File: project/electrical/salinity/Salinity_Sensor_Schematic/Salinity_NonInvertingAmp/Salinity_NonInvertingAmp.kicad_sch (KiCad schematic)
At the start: 13 parts, among them U1 MCP6L01, U2 MCP6L01, U3 MCP6L01

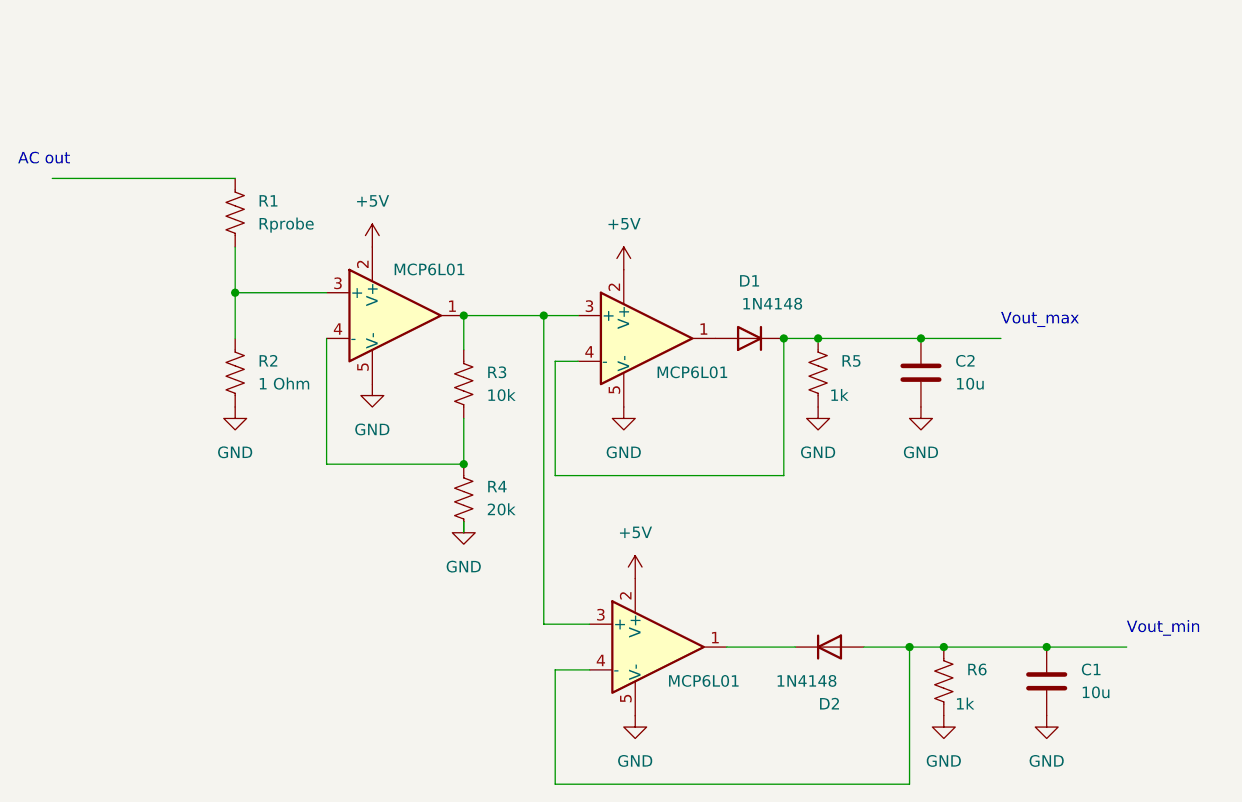
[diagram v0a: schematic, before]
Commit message: circuit updates and simulations
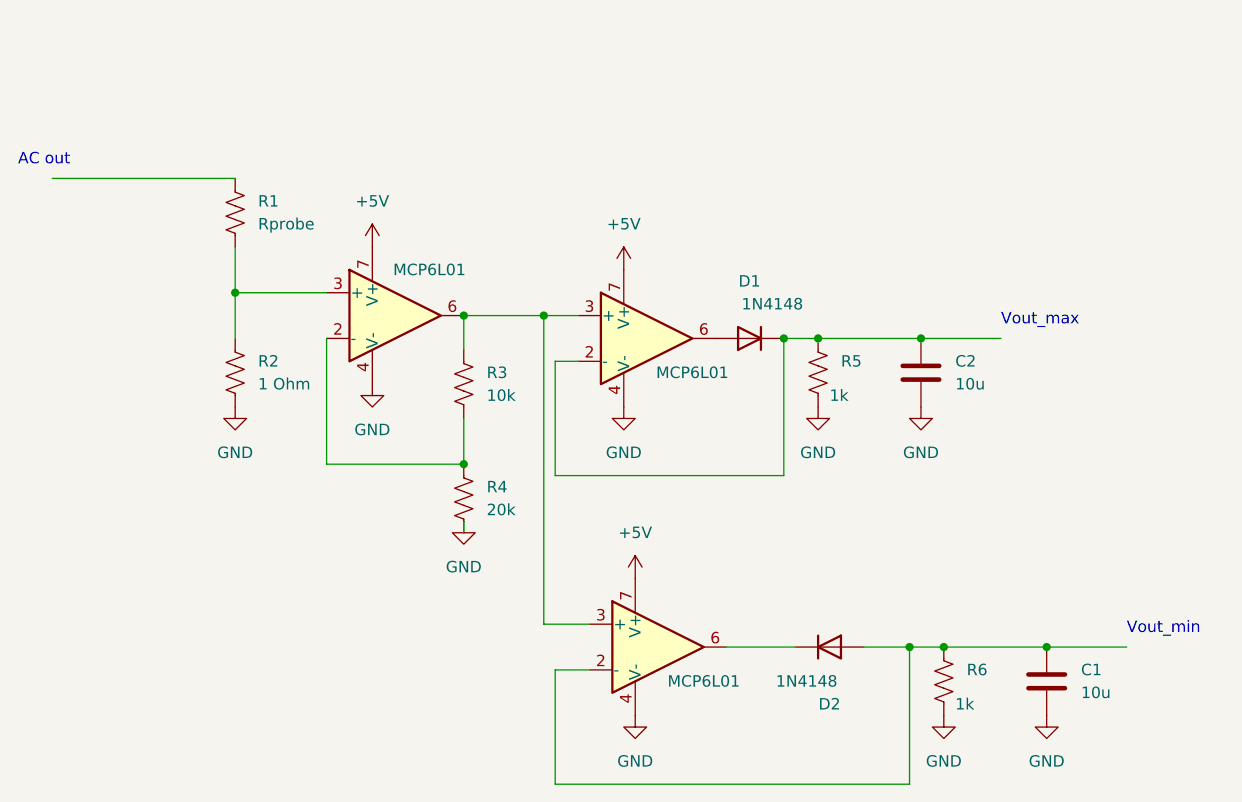
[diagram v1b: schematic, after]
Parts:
- U1, U2, U3: footprint Package_TO_SOT_SMD:SOT-23-5 -> Package_SO:TSSOP-8_4.4x3mm_P0.65mm; symbol Amplifier_Operational:MCP6L01Rx-xOT -> Amplifier_Operational:MCP601-xST
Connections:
- net +5V: now also U1.7 (V+), U2.7 (V+), U3.7 (V+); no longer U1.2 (V+), U2.2 (V+), U3.2 (V+)
- net GND: now also U1.4 (V-), U2.4 (V-), U3.4 (V-); no longer U1.5 (V-), U2.5 (V-), U3.5 (V-)
- net at C2.1, D1.1 (K), R5.1: now also U2.2 (-); no longer U2.4 (-)
- net at D1.2 (A): now also U2.6; no longer U2.1
- net at R3.1, U2.3 (+), U3.3 (+): now also U1.6; no longer U1.1
- net at R3.2, R4.1: now also U1.2 (-); no longer U1.4 (-)
- net at U3.1 (NC): no longer D2.1 (K)
- net at C1.1, D2.2 (A), R6.1: now also U3.2 (-); no longer U3.4 (-)
- new net: D2.1 (K), U3.6
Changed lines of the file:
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@@
     )
   )
-  (symbol (lib_id "Amplifier_Operational:MCP6L01Rx-xOT") (at 109.22 123.19 0) (unit 1)
+  (symbol (lib_id "Amplifier_Operational:MCP601-xST") (at 109.22 123.19 0) (unit 1)
     (in_bom yes) (on_board yes) (dnp no)
     (property "Reference" "U3" (at 123.19 118.9991 0)
@@
       (effects (font (size 1.27 1.27)))
     )
-    (property "Footprint" "Package_TO_SOT_SMD:SOT-23-5" (at 109.22 123.19 0)
-      (effects (font (size 1.27 1.27)) hide)
+    (property "Footprint" "Package_SO:TSSOP-8_4.4x3mm_P0.65mm" (at 106.68 128.27 0)
+      (effects (font (size 1.27 1.27)) (justify left) hide)
     )
-    (property "Datasheet" "http://ww1.microchip.com/downloads/en/devicedoc/22140b.pdf" (at 109.22 118.11 0)
+    (property "Datasheet" "http://ww1.microchip.com/downloads/en/DeviceDoc/21314g.pdf" (at 113.03 119.38 0)
       (effects (font (size 1.27 1.27)) hide)
     )
@@
     (pin "5")
     (pin "2")
+    (pin "8")
+    (pin "6")
+    (pin "7")
     (instances
       (project "Salinity_NonInvertingAmp"
@@
     )
   )
-  (symbol (lib_id "Amplifier_Operational:MCP6L01Rx-xOT") (at 107.95 88.9 0) (unit 1)
+  (symbol (lib_id "Amplifier_Operational:MCP601-xST") (at 107.95 88.9 0) (unit 1)
     (in_bom yes) (on_board yes) (dnp no)
     (property "Reference" "U2" (at 121.92 84.7091 0)
@@
       (effects (font (size 1.27 1.27)))
     )
-    (property "Footprint" "Package_TO_SOT_SMD:SOT-23-5" (at 107.95 88.9 0)
-      (effects (font (size 1.27 1.27)) hide)
+    (property "Footprint" "Package_SO:TSSOP-8_4.4x3mm_P0.65mm" (at 105.41 93.98 0)
+      (effects (font (size 1.27 1.27)) (justify left) hide)
     )
-    (property "Datasheet" "http://ww1.microchip.com/downloads/en/devicedoc/22140b.pdf" (at 107.95 83.82 0)
+    (property "Datasheet" "http://ww1.microchip.com/downloads/en/DeviceDoc/21314g.pdf" (at 111.76 85.09 0)
       (effects (font (size 1.27 1.27)) hide)
     )
@@
     (pin "5")
     (pin "2")
+    (pin "7")
+    (pin "8")
+    (pin "6")
     (instances
       (project "Salinity_NonInvertingAmp"
@@
     )
   )
-  (symbol (lib_id "Amplifier_Operational:MCP6L01Rx-xOT") (at 80.01 86.36 0) (unit 1)
+  (symbol (lib_id "Amplifier_Operational:MCP601-xST") (at 80.01 86.36 0) (unit 1)
     (in_bom yes) (on_board yes) (dnp no)
     (property "Reference" "U1" (at 93.98 82.1691 0)
@@
       (effects (font (size 1.27 1.27)))
     )
-    (property "Footprint" "Package_TO_SOT_SMD:SOT-23-5" (at 80.01 86.36 0)
-      (effects (font (size 1.27 1.27)) hide)
+    (property "Footprint" "Package_SO:TSSOP-8_4.4x3mm_P0.65mm" (at 77.47 91.44 0)
+      (effects (font (size 1.27 1.27)) (justify left) hide)
     )
-    (property "Datasheet" "http://ww1.microchip.com/downloads/en/devicedoc/22140b.pdf" (at 80.01 81.28 0)
+    (property "Datasheet" "http://ww1.microchip.com/downloads/en/DeviceDoc/21314g.pdf" (at 83.82 82.55 0)
       (effects (font (size 1.27 1.27)) hide)
     )
@@
     (pin "2")
     (pin "1")
+    (pin "7")
+    (pin "6")
+    (pin "8")
     (instances
       (project "Salinity_NonInvertingAmp"

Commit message: updated salinity
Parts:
- C1, C2: value 10u -> 10n
- R5, R6: value 1k -> 1M
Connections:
- net +5V: now also C1.1, R6.1
- net GND: no longer C1.2, R6.2
- net at D2.2 (A), U3.2 (-): now also C1.2, R6.2; no longer C1.1, R6.1
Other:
- moved on the sheet: C1, R6
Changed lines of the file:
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@@
   (junction (at 137.16 123.19) (diameter 0) (color 0 0 0 0)
   )
+  (junction (at 148.59 123.19) (diameter 0) (color 0 0 0 0)
+  )
   (junction (at 96.52 86.36) (diameter 0) (color 0 0 0 0)
   )
@@
   (junction (at 127 88.9) (diameter 0) (color 0 0 0 0)
   )
-  (junction (at 152.4 123.19) (diameter 0) (color 0 0 0 0)
-  )
-  (junction (at 140.97 123.19) (diameter 0) (color 0 0 0 0)
-  )
   (junction (at 138.43 88.9) (diameter 0) (color 0 0 0 0)
   )
@@
     (stroke (width 0) (type default))
   )
-  (wire (pts (xy 137.16 123.19) (xy 140.97 123.19))
-    (stroke (width 0) (type default))
-  )
   (wire (pts (xy 87.63 90.17) (xy 87.63 86.36))
     (stroke (width 0) (type default))
@@
     (stroke (width 0) (type default))
   )
-  (wire (pts (xy 152.4 123.19) (xy 161.29 123.19))
-    (stroke (width 0) (type default))
-  )
   (wire (pts (xy 62.23 83.82) (xy 72.39 83.82))
     (stroke (width 0) (type default))
@@
     (stroke (width 0) (type default))
   )
+  (wire (pts (xy 137.16 123.19) (xy 148.59 123.19))
+    (stroke (width 0) (type default))
+  )
   (wire (pts (xy 97.79 91.44) (xy 100.33 91.44))
     (stroke (width 0) (type default))
   )
-  (wire (pts (xy 140.97 123.19) (xy 152.4 123.19))
-    (stroke (width 0) (type default))
-  )
   (wire (pts (xy 97.79 91.44) (xy 97.79 104.14))
+    (stroke (width 0) (type default))
+  )
+  (wire (pts (xy 148.59 123.19) (xy 161.29 123.19))
     (stroke (width 0) (type default))
   )
@@
     )
   )
+  (symbol (lib_id "power:+5V") (at 137.16 115.57 0) (unit 1)
+    (in_bom yes) (on_board yes) (dnp no) (fields_autoplaced)
+    (property "Reference" "#PWR011" (at 137.16 119.38 0)
+      (effects (font (size 1.27 1.27)) hide)
+    )
+    (property "Value" "+5V" (at 137.16 110.49 0)
+      (effects (font (size 1.27 1.27)))
+    )
+    (property "Footprint" "" (at 137.16 115.57 0)
+      (effects (font (size 1.27 1.27)) hide)
+    )
+    (property "Datasheet" "" (at 137.16 115.57 0)
+      (effects (font (size 1.27 1.27)) hide)
+    )
+    (pin "1")
+    (instances
+      (project "Salinity_NonInvertingAmp"
+        (path "/c65a21d9-20a5-4e14-a1e3-194a093334b0"
+          (reference "#PWR011") (unit 1)
+        )
+      )
+    )
+  )
   (symbol (lib_id "Amplifier_Operational:MCP601-xST") (at 107.95 88.9 0) (unit 1)
     (in_bom yes) (on_board yes) (dnp no)
@@
     )
   )
+  (symbol (lib_id "power:+5V") (at 148.59 115.57 0) (unit 1)
+    (in_bom yes) (on_board yes) (dnp no) (fields_autoplaced)
+    (property "Reference" "#PWR012" (at 148.59 119.38 0)
+      (effects (font (size 1.27 1.27)) hide)
+    )
+    (property "Value" "+5V" (at 148.59 110.49 0)
+      (effects (font (size 1.27 1.27)))
+    )
+    (property "Footprint" "" (at 148.59 115.57 0)
+      (effects (font (size 1.27 1.27)) hide)
+    )
+    (property "Datasheet" "" (at 148.59 115.57 0)
+      (effects (font (size 1.27 1.27)) hide)
+    )
+    (pin "1")
+    (instances
+      (project "Salinity_NonInvertingAmp"
+        (path "/c65a21d9-20a5-4e14-a1e3-194a093334b0"
+          (reference "#PWR012") (unit 1)
+        )
+      )
+    )
+  )
   (symbol (lib_id "power:GND") (at 138.43 96.52 0) (unit 1)
     (in_bom yes) (on_board yes) (dnp no) (fields_autoplaced)
@@
     )
   )
-  (symbol (lib_id "power:GND") (at 152.4 130.81 0) (unit 1)
-    (in_bom yes) (on_board yes) (dnp no) (fields_autoplaced)
-    (property "Reference" "#PWR012" (at 152.4 137.16 0)
-      (effects (font (size 1.27 1.27)) hide)
-    )
-    (property "Value" "GND" (at 152.4 135.89 0)
-      (effects (font (size 1.27 1.27)))
-    )
-    (property "Footprint" "" (at 152.4 130.81 0)
-      (effects (font (size 1.27 1.27)) hide)
-    )
-    (property "Datasheet" "" (at 152.4 130.81 0)
-      (effects (font (size 1.27 1.27)) hide)
-    )
-    (pin "1")
-    (instances
-      (project "Salinity_NonInvertingAmp"
-        (path "/c65a21d9-20a5-4e14-a1e3-194a093334b0"
-          (reference "#PWR012") (unit 1)
-        )
-      )
-    )
-  )
   (symbol (lib_id "Device:R_US") (at 62.23 74.93 0) (unit 1)
     (in_bom yes) (on_board yes) (dnp no) (fields_autoplaced)
@@
     )
   )
-  (symbol (lib_id "Device:C") (at 152.4 127 0) (unit 1)
-    (in_bom yes) (on_board yes) (dnp no) (fields_autoplaced)
-    (property "Reference" "C1" (at 156.21 125.73 0)
-      (effects (font (size 1.27 1.27)) (justify left))
-    )
-    (property "Value" "10u" (at 156.21 128.27 0)
-      (effects (font (size 1.27 1.27)) (justify left))
-    )
-    (property "Footprint" "" (at 153.3652 130.81 0)
-      (effects (font (size 1.27 1.27)) hide)
-    )
-    (property "Datasheet" "~" (at 152.4 127 0)
+  (symbol (lib_id "Device:C") (at 148.59 119.38 0) (unit 1)
+    (in_bom yes) (on_board yes) (dnp no) (fields_autoplaced)
+    (property "Reference" "C1" (at 152.4 118.11 0)
+      (effects (font (size 1.27 1.27)) (justify left))
+    )
+    (property "Value" "10n" (at 152.4 120.65 0)
+      (effects (font (size 1.27 1.27)) (justify left))
+    )
+    (property "Footprint" "" (at 149.5552 123.19 0)
+      (effects (font (size 1.27 1.27)) hide)
+    )
+    (property "Datasheet" "~" (at 148.59 119.38 0)
       (effects (font (size 1.27 1.27)) hide)
     )
@@
     )
   )
-  (symbol (lib_id "Device:R_US") (at 140.97 127 0) (unit 1)
+  (symbol (lib_id "Device:R_US") (at 137.16 119.38 0) (unit 1)
     (in_bom yes) (on_board yes) (dnp no)
-    (property "Reference" "R6" (at 143.51 125.73 0)
-      (effects (font (size 1.27 1.27)) (justify left))
-    )
-    (property "Value" "1k" (at 142.24 129.54 0)
-      (effects (font (size 1.27 1.27)) (justify left))
-    )
-    (property "Footprint" "" (at 141.986 127.254 90)
-      (effects (font (size 1.27 1.27)) hide)
-    )
-    (property "Datasheet" "~" (at 140.97 127 0)
+    (property "Reference" "R6" (at 139.7 118.11 0)
+      (effects (font (size 1.27 1.27)) (justify left))
+    )
+    (property "Value" "1M" (at 138.43 121.92 0)
+      (effects (font (size 1.27 1.27)) (justify left))
+    )
+    (property "Footprint" "" (at 138.176 119.634 90)
+      (effects (font (size 1.27 1.27)) hide)
+    )
+    (property "Datasheet" "~" (at 137.16 119.38 0)
       (effects (font (size 1.27 1.27)) hide)
     )
@@
         (path "/c65a21d9-20a5-4e14-a1e3-194a093334b0"
           (reference "#PWR03") (unit 1)
-        )
-      )
-    )
-  )
-  (symbol (lib_id "power:GND") (at 140.97 130.81 0) (unit 1)
-    (in_bom yes) (on_board yes) (dnp no) (fields_autoplaced)
-    (property "Reference" "#PWR011" (at 140.97 137.16 0)
-      (effects (font (size 1.27 1.27)) hide)
-    )
-    (property "Value" "GND" (at 140.97 135.89 0)
-      (effects (font (size 1.27 1.27)))
-    )
-    (property "Footprint" "" (at 140.97 130.81 0)
-      (effects (font (size 1.27 1.27)) hide)
-    )
-    (property "Datasheet" "" (at 140.97 130.81 0)
-      (effects (font (size 1.27 1.27)) hide)
-    )
-    (pin "1")
-    (instances
-      (project "Salinity_NonInvertingAmp"
-        (path "/c65a21d9-20a5-4e14-a1e3-194a093334b0"
-          (reference "#PWR011") (unit 1)
         )
       )
@@
       (effects (font (size 1.27 1.27)) (justify left))
     )
-    (property "Value" "10u" (at 142.24 93.98 0)
+    (property "Value" "10n" (at 142.24 93.98 0)
       (effects (font (size 1.27 1.27)) (justify left))
     )
@@
       (effects (font (size 1.27 1.27)) (justify left))
     )
-    (property "Value" "1k" (at 128.27 95.25 0)
-      (effects (font (size 1.27 1.27)) (justify left))
-    )
+    (property "Value" "1M" (at 128.27 95.25 0)
+      (effects (font (size 1.27 1.27)) (justify left))
+    )

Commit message: Made some circuits better for overleaf
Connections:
- net GND: now also R4.1; no longer R4.2
- net at R3.2, U1.2 (-): now also R4.2; no longer R4.1
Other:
- moved on the sheet: C1, D2, R1, R2, R3, R4, R6
